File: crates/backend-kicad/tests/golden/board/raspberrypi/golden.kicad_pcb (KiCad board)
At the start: 2 copper layers, 100 x 80 mm, 1 part, among them U1 U

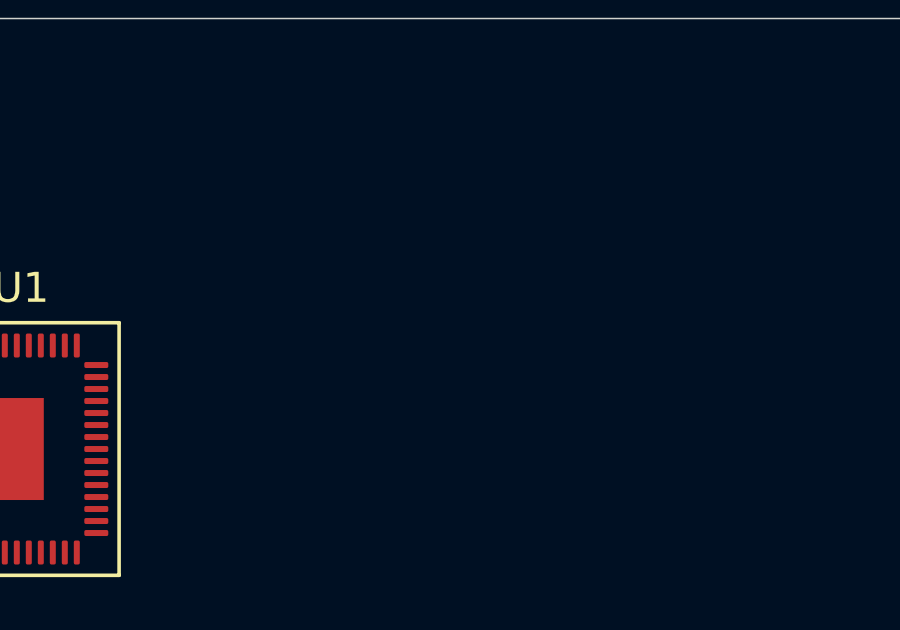
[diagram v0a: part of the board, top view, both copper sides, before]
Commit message: Improve recognition of bypass caps
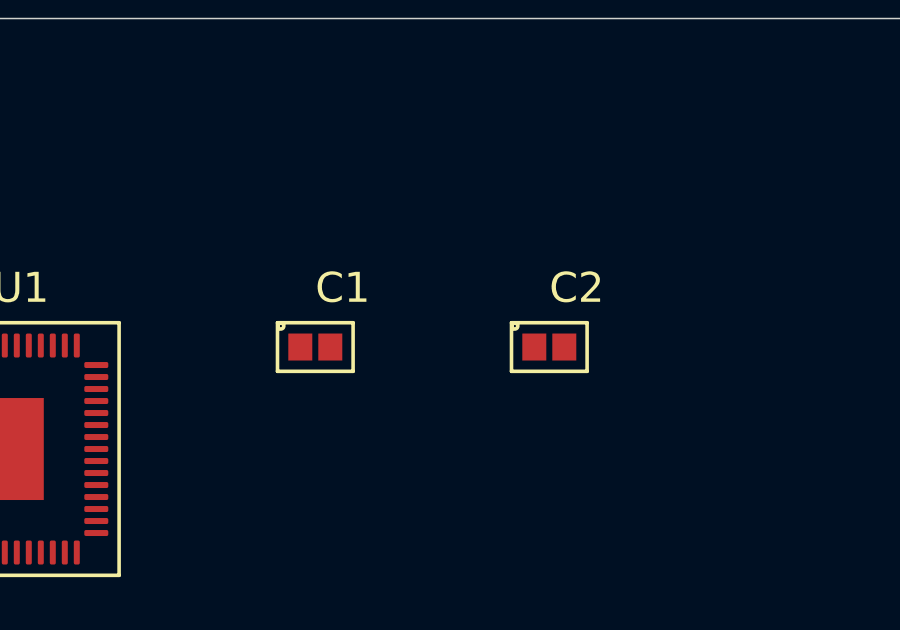
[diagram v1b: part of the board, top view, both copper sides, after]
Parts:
- added C1: C, Capacitor_SMD.3dshapes/C_0603_1608Metric, F.Cu at (25.1, 10.9)
- added C2: C, Capacitor_SMD.3dshapes/C_0603_1608Metric, F.Cu at (32.9, 10.9)
